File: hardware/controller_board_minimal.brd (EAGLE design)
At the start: 51 x 58.5 mm, 61 parts, among them J4 AVR_SPI_PRG_6NS, J8 FRSKY-GIMBAL-2X-SERVO, J9 FRSKY-GIMBAL-2X-SERVO, P1 TEST-POINT, P2 TEST-POINT, P3 TEST-POINT, P4 TEST-POINT, U1 ATMEGA128RFA1, U5 3.3V, Y1 CRYSTAL5X3

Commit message: small tweaks; final routing; rc5
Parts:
- moved V19 15.5 mm to (-4.50, 17.8)
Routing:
- net GND: track 30.2 -> 30.9 mm
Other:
- board text added: "For 50 boards, this is $1.66/board"
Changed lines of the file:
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@@
 <drawing>
 <settings>
-<setting alwaysvectorfont="no"/>
+<setting alwaysvectorfont="yes"/>
 <setting verticaltext="up"/>
 </settings>
-<grid distance="0.5" unitdist="mm" unit="mm" style="lines" multiple="1" display="no" altdistance="5" altunitdist="mil" altunit="mil"/>
+<grid distance="0.25" unitdist="mm" unit="mm" style="lines" multiple="1" display="no" altdistance="5" altunitdist="mil" altunit="mil"/>
 <layers>
 <layer number="1" name="Top" color="4" fill="1" visible="yes" active="yes"/>
@@
 <text x="-5.375" y="-20.875" size="1.778" layer="21" font="vector" rot="R180" align="center">on</text>
 <text x="3.125" y="-20.75" size="1.778" layer="21" font="vector" rot="R180" align="center">off</text>
-<text x="17" y="-30.125" size="1.778" layer="21" font="vector" rot="R180">reset</text>
+<text x="13.5" y="-17.125" size="1.778" layer="21" font="vector" rot="R180">reset</text>
 <wire x1="-9" y1="20" x2="-9" y2="15" width="0.127" layer="41"/>
 <wire x1="-9" y1="15" x2="-1.6875" y2="15" width="0.127" layer="41"/>
@@
 <wire x1="0.625" y1="15" x2="0.625" y2="14.25" width="0.127" layer="41"/>
 <text x="-8.25" y="20.8125" size="0.7" layer="21" font="vector">Rev 2</text>
+<text x="-34.5" y="41.75" size="3" layer="48" font="vector">For 50 boards, this is $1.66/board</text>
 </plain>
 <attributes>
@@
 <attribute name="DISTPN" value="NA" x="3.625" y="19.5" size="1.778" layer="27" display="off"/>
 </element>
-<element name="V19" library="quadparts_prebuilt" package="VIA-0.2MM" value="LOCKED-VIA-0.2" x="-17.25" y="26.5">
-<attribute name="CREATOR" value="Swanson" x="-17.25" y="26.5" size="1.778" layer="27" display="off"/>
-<attribute name="DIST" value="NA" x="-17.25" y="26.5" size="1.778" layer="27" display="off"/>
-<attribute name="DISTPN" value="NA" x="-17.25" y="26.5" size="1.778" layer="27" display="off"/>
+<element name="V19" library="quadparts_prebuilt" package="VIA-0.2MM" value="LOCKED-VIA-0.2" x="-4.5" y="17.75">
+<attribute name="CREATOR" value="Swanson" x="-4.5" y="17.75" size="1.778" layer="27" display="off"/>
+<attribute name="DIST" value="NA" x="-4.5" y="17.75" size="1.778" layer="27" display="off"/>
+<attribute name="DISTPN" value="NA" x="-4.5" y="17.75" size="1.778" layer="27" display="off"/>
 </element>
 <element name="F2" library="RemoteParts" package="FIDUCIAL_STENCIL" value="1mm" x="10.125" y="-15.8375" smashed="yes">
@@
 <via x="-6.5" y="8.6" extent="1-16" drill="0.2"/>
 <wire x1="4.551" y1="10.57" x2="4.581" y2="10.6" width="0.254" layer="1"/>
-<wire x1="4.581" y1="10.6" x2="5.6" y2="10.6" width="0.254" layer="1"/>
-<via x="5.6" y="10.6" extent="1-16" drill="0.2"/>
 <wire x1="4.551" y1="9.07" x2="5.67" y2="9.07" width="0.254" layer="1"/>
 <wire x1="5.67" y1="9.07" x2="5.9" y2="9.3" width="0.254" layer="1"/>
@@
 <wire x1="5.83" y1="7.57" x2="6.1" y2="7.3" width="0.254" layer="1"/>
 <via x="6.1" y="7.3" extent="1-16" drill="0.2"/>
-<wire x1="1.92" y1="3.439" x2="1.92" y2="4.78" width="0.254" layer="1"/>
 <wire x1="1.92" y1="4.78" x2="1.9" y2="4.8" width="0.254" layer="1"/>
-<via x="1.9" y="4.8" extent="1-16" drill="0.2"/>
 <wire x1="13.125" y1="6.645" x2="13.125" y2="8.175" width="0.254" layer="1"/>
 <wire x1="13.125" y1="8.175" x2="13.1" y2="8.2" width="0.254" layer="1"/>
@@
 <wire x1="-3.08" y1="4.3134" x2="-2.794" y2="4.5994" width="0.254" layer="1"/>
 <via x="-2.794" y="4.5994" extent="1-16" drill="0.2"/>
+<wire x1="1.92" y1="3.439" x2="1.92" y2="4.587" width="0.254" layer="1"/>
+<wire x1="1.92" y1="4.587" x2="2.413" y2="5.08" width="0.254" layer="1"/>
+<via x="2.413" y="5.08" extent="1-16" drill="0.2"/>
+<wire x1="4.551" y1="10.57" x2="5.6764" y2="10.57" width="0.254" layer="1"/>
+<wire x1="5.6764" y1="10.57" x2="5.75" y2="10.6436" width="0.254" layer="1"/>
+<via x="5.75" y="10.6436" extent="1-16" drill="0.2"/>
 </signal>
 <signal name="BTN1">
@@
 <wire x1="-5" y1="-5.54" x2="-5" y2="-5.75" width="0.1524" layer="16"/>
 <via x="5.75" y="11.25" extent="1-16" drill="0.2"/>
-<wire x1="5.41128125" y1="11.0556" x2="5.5556" y2="11.0556" width="0.1524" layer="16"/>
-<wire x1="5.5556" y1="11.0556" x2="5.75" y2="11.25" width="0.1524" layer="16"/>
-<wire x1="-3.25" y1="2.39431875" x2="5.41128125" y2="11.0556" width="0.1524" layer="16"/>
 <wire x1="-3.25" y1="-4" x2="-3.25" y2="2.39431875" width="0.1524" layer="16"/>
+<wire x1="5.5992" y1="11.0992" x2="5.75" y2="11.25" width="0.1524" layer="16"/>
+<wire x1="5.45488125" y1="11.0992" x2="5.5992" y2="11.0992" width="0.1524" layer="16"/>
+<wire x1="-3.25" y1="2.39431875" x2="5.45488125" y2="11.0992" width="0.1524" layer="16"/>
 </signal>
 <signal name="3V3" class="1">
@@
 <wire x1="4.75" y1="10" x2="5.25" y2="10" width="0.1524" layer="1"/>
 <wire x1="4.551" y1="10.07" x2="4.75" y2="10" width="0.1524" layer="1"/>
-<wire x1="5.78871875" y1="10.1444" x2="6.0556" y2="10.41128125" width="0.1524" layer="1"/>
 <wire x1="5.25" y1="10" x2="5.3944" y2="10.1444" width="0.1524" layer="1"/>
-<wire x1="6.0556" y1="10.8056" x2="7.25" y2="12" width="0.1524" layer="1"/>
-<wire x1="5.3944" y1="10.1444" x2="5.78871875" y2="10.1444" width="0.1524" layer="1"/>
-<wire x1="6.0556" y1="10.41128125" x2="6.0556" y2="10.8056" width="0.1524" layer="1"/>
+<wire x1="6.2056" y1="10.9556" x2="7.25" y2="12" width="0.1524" layer="1"/>
+<wire x1="6.2056" y1="10.45488125" x2="6.2056" y2="10.9556" width="0.1524" layer="1"/>
+<wire x1="5.89511875" y1="10.1444" x2="6.2056" y2="10.45488125" width="0.1524" layer="1"/>
+<wire x1="5.3944" y1="10.1444" x2="5.89511875" y2="10.1444" width="0.1524" layer="1"/>
 </signal>
 <signal name="N$7">

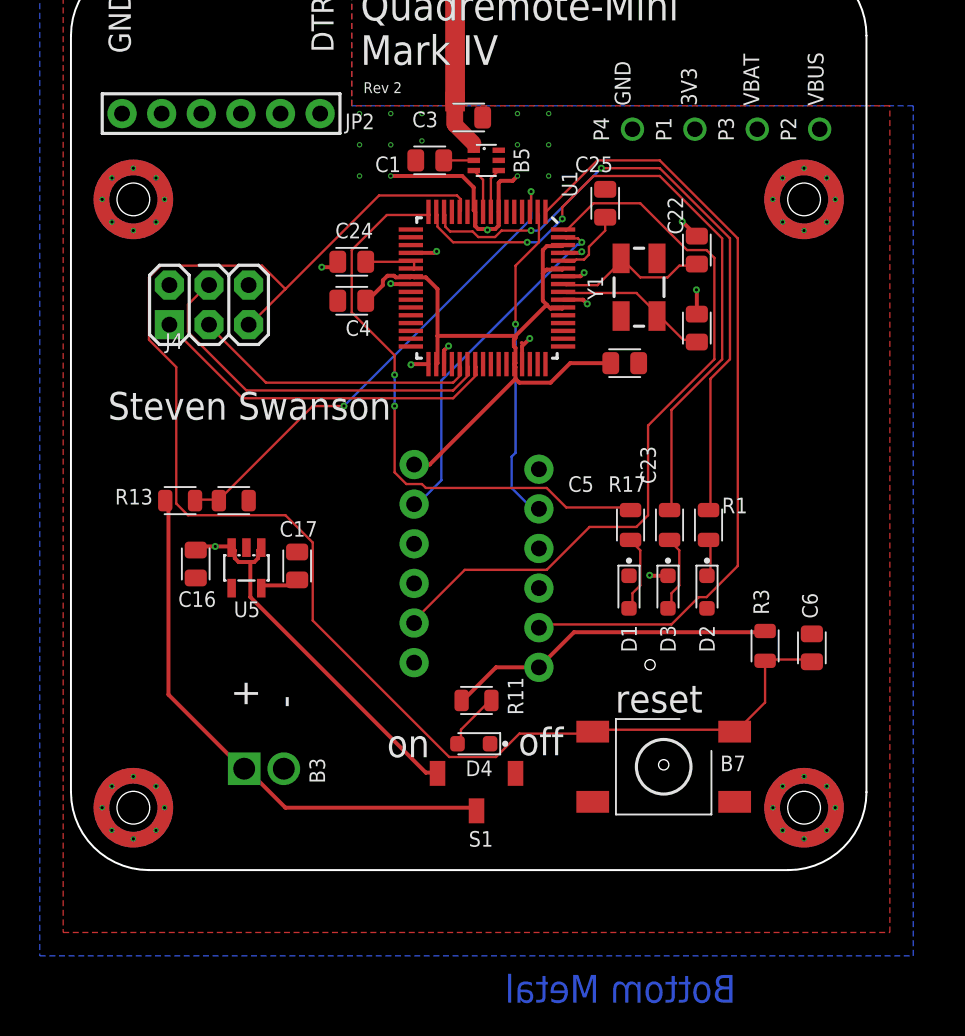
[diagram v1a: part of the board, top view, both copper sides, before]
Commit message: notes from undergrads.  Tweak stencil fiducial. Some new parts
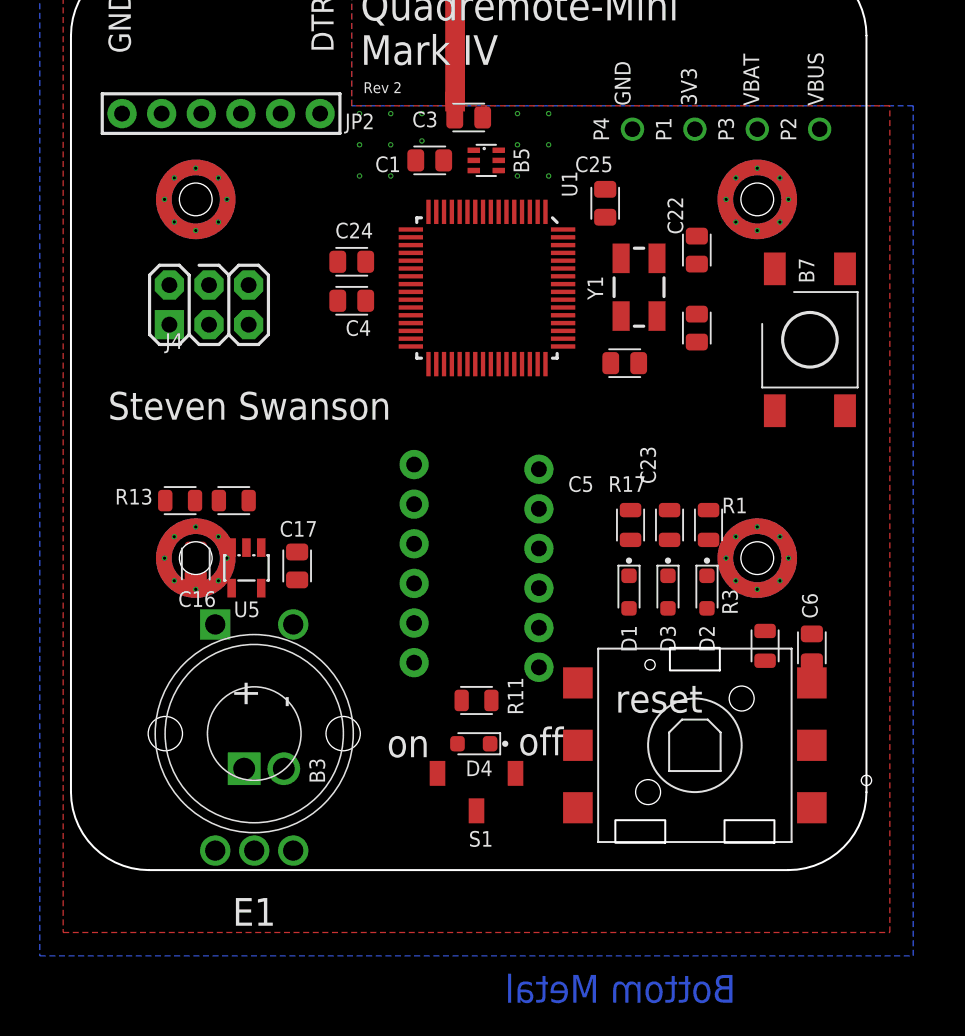
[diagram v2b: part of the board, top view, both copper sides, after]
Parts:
- added E1: ROTARY-ENCODER-W/BUTTON-BOURNS-PEC12R-30MM, RemoteParts:BOURNS-PEC12R
- added U$4: NAV-SWITCH, RemoteParts:NAV-SWITCH-JS5208
- moved B7 28.9 mm to (20.4, 5.00), turned to 0 degrees
- moved U$1 16.5 mm to (-19.0, -9.00)
- moved U$2 16.3 mm to (17.0, -9.00)
- moved F4 13.0 mm to (24.0, -23.2)
- moved U$3 4.00 mm to (-19.0, 14.0)
- moved U$6 3.00 mm to (17.0, 14.0)
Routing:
- net RESET: track 97.8 -> 0.00 mm
- net 3V3: track 65.9 -> 0.00 mm
- net ROLL: track 51.3 -> 0.00 mm
- net THROTTLE: track 48.1 -> 0.00 mm
- net N$4: track 42.3 -> 0.00 mm, vias 2 -> 0
- net N$8: track 41.2 -> 0.00 mm, vias 2 -> 0
- net N$16: track 37.7 -> 0.00 mm, vias 2 -> 0
- net BPOS: track 35.5 -> 0.00 mm
- net BAT_SENSE: track 32.2 -> 0.00 mm, vias 2 -> 0
- net GND: track 30.9 -> 0.00 mm, vias 13 -> 0
- net VBAT: track 24.8 -> 0.00 mm, vias 1 -> 0
- net MOSI: track 24.3 -> 0.00 mm
- net YAW: track 23.1 -> 0.00 mm, vias 1 -> 0
- net MISO: track 23.0 -> 0.00 mm
- net PITCH: track 20.8 -> 0.00 mm, vias 1 -> 0
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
